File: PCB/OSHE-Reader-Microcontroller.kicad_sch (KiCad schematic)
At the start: 3 parts

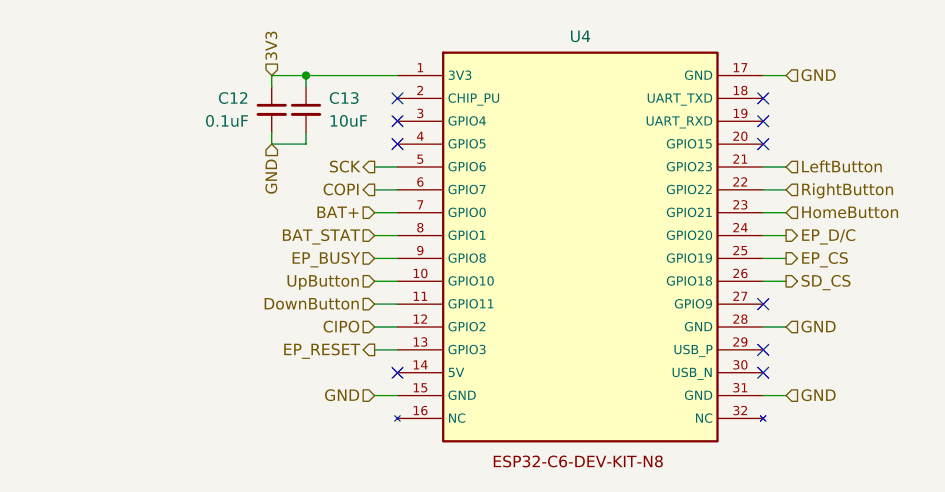
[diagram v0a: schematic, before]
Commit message: fixed battery voltage input to mcu being over 3.3V, minor changes to layout of sd card schematic
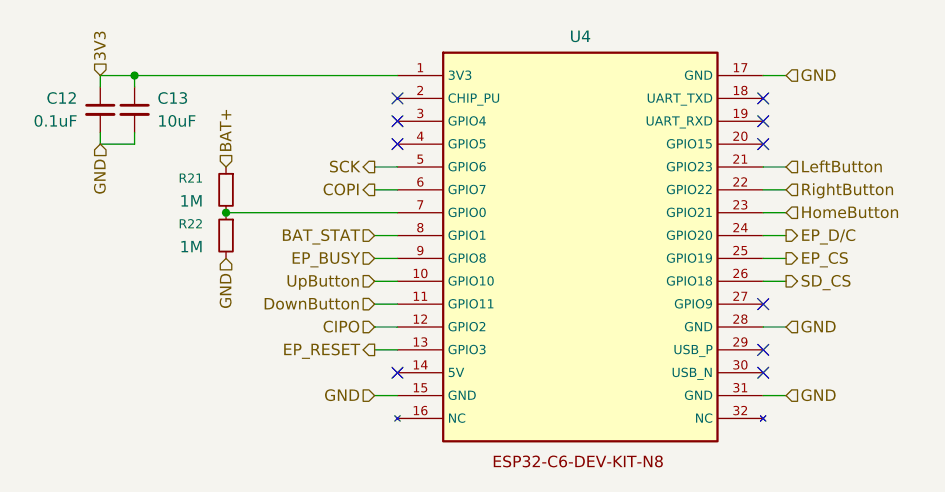
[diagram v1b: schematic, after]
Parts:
- added R21, R22: 1M, symbol Device:R_Small
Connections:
- net BAT+: now also R21.1; no longer U4.7 (GPIO0)
- net GND: now also R22.2
- new net: R21.2, R22.1, U4.7 (GPIO0)
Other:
- moved on the sheet: C12, C13
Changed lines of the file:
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@@
 	(paper "A4")
 	(junction
-		(at 53.34 49.53)
+		(at 34.29 49.53)
 		(diameter 0)
 		(color 0 0 0 0)
 	)
+	(junction
+		(at 44.45 64.77)
+		(diameter 0)
+		(color 0 0 0 0)
+	)
 	(no_connect
 		(at 63.5 54.61)
@@
 	(wire
 		(pts
-			(xy 49.53 49.53) (xy 53.34 49.53)
+			(xy 30.48 49.53) (xy 34.29 49.53)
 		)
 		(stroke
@@
 	(wire
 		(pts
-			(xy 53.34 50.8) (xy 53.34 49.53)
-		)
-		(stroke
-			(width 0)
-			(type default)
-		)
-	)
-	(wire
-		(pts
-			(xy 49.53 57.15) (xy 53.34 57.15)
+			(xy 34.29 50.8) (xy 34.29 49.53)
+		)
+		(stroke
+			(width 0)
+			(type default)
+		)
+	)
+	(wire
+		(pts
+			(xy 30.48 57.15) (xy 34.29 57.15)
 		)
 		(stroke
@@
 	(wire
 		(pts
+			(xy 44.45 64.77) (xy 63.5 64.77)
+		)
+		(stroke
+			(width 0)
+			(type default)
+		)
+	)
+	(wire
+		(pts
 			(xy 60.96 72.39) (xy 63.5 72.39)
 		)
@@
 	(wire
 		(pts
-			(xy 60.96 64.77) (xy 63.5 64.77)
-		)
-		(stroke
-			(width 0)
-			(type default)
-		)
-	)
-	(wire
-		(pts
 			(xy 60.96 62.23) (xy 63.5 62.23)
 		)
@@
 	(wire
 		(pts
-			(xy 49.53 57.15) (xy 49.53 55.88)
+			(xy 30.48 57.15) (xy 30.48 55.88)
 		)
 		(stroke
@@
 	(wire
 		(pts
-			(xy 49.53 50.8) (xy 49.53 49.53)
+			(xy 30.48 50.8) (xy 30.48 49.53)
 		)
 		(stroke
@@
 	(wire
 		(pts
-			(xy 53.34 57.15) (xy 53.34 55.88)
+			(xy 34.29 57.15) (xy 34.29 55.88)
 		)
 		(stroke
@@
 	(wire
 		(pts
-			(xy 53.34 49.53) (xy 63.5 49.53)
+			(xy 34.29 49.53) (xy 63.5 49.53)
 		)
 		(stroke
@@
 	(hierarchical_label "GND"
 		(shape input)
-		(at 49.53 57.15 270)
+		(at 30.48 57.15 270)
 		(effects
 			(font
@@
 	(hierarchical_label "BAT+"
 		(shape input)
-		(at 60.96 64.77 180)
-		(effects
-			(font
-				(size 1.27 1.27)
-			)
-			(justify right)
+		(at 44.45 59.69 90)
+		(effects
+			(font
+				(size 1.27 1.27)
+			)
+			(justify left)
 		)
 	)
@@
 	(hierarchical_label "3V3"
 		(shape input)
-		(at 49.53 49.53 90)
+		(at 30.48 49.53 90)
 		(effects
 			(font
@@
 		(shape output)
 		(at 60.96 59.69 180)
+		(effects
+			(font
+				(size 1.27 1.27)
+			)
+			(justify right)
+		)
+	)
+	(hierarchical_label "GND"
+		(shape input)
+		(at 44.45 69.85 270)
 		(effects
 			(font
@@
 	(symbol
 		(lib_id "Device:C_Small")
-		(at 49.53 53.34 0)
+		(at 30.48 53.34 0)
 		(mirror y)
 		(unit 1)
@@
 		(dnp no)
 		(property "Reference" "C12"
-			(at 46.99 52.0762 0)
+			(at 27.94 52.0762 0)
 			(effects
 				(font
@@
 		)
 		(property "Value" "0.1uF"
-			(at 46.99 54.6162 0)
+			(at 27.94 54.6162 0)
 			(effects
 				(font
@@
 		)
 		(property "Footprint" ""
-			(at 49.53 53.34 0)
+			(at 30.48 53.34 0)
 			(effects
 				(font
@@
 		)
 		(property "Datasheet" "~"
-			(at 49.53 53.34 0)
+			(at 30.48 53.34 0)
 			(effects
 				(font
@@
 		)
 		(property "Description" "Unpolarized capacitor, small symbol"
-			(at 49.53 53.34 0)
+			(at 30.48 53.34 0)
 			(effects
 				(font
@@
 	)
 	(symbol
+		(lib_id "Device:R_Small")
+		(at 44.45 67.31 0)
+		(mirror y)
+		(unit 1)
+		(exclude_from_sim no)
+		(in_bom yes)
+		(on_board yes)
+		(dnp no)
+		(property "Reference" "R22"
+			(at 41.91 66.0399 0)
+			(effects
+				(font
+					(size 1.016 1.016)
+				)
+				(justify left)
+			)
+		)
+		(property "Value" "1M"
+			(at 41.91 68.5799 0)
+			(effects
+				(font
+					(size 1.27 1.27)
+				)
+				(justify left)
+			)
+		)
+		(property "Footprint" ""
+			(at 44.45 67.31 0)
+			(effects
+				(font
+					(size 1.27 1.27)
+				)
+				(hide yes)
+			)
+		)
+		(property "Datasheet" "~"
+			(at 44.45 67.31 0)
+			(effects
+				(font
+					(size 1.27 1.27)
+				)
+				(hide yes)
+			)
+		)
+		(property "Description" "Resistor, small symbol"
+			(at 44.45 67.31 0)
+			(effects
+				(font
+					(size 1.27 1.27)
+				)
+				(hide yes)
+			)
+		)
+		(pin "1"
+		)
+		(pin "2"
+		)
+		(instances
+			(project "OSHE-Reader-PCB"
+				(path "/3f072c92-e35a-4654-839b-728bd3dc3a46/03424bf7-051b-4358-a08a-8020da2e6def"
+					(reference "R22")
+					(unit 1)
+				)
+			)
+		)
+	)
+	(symbol
+		(lib_id "Device:R_Small")
+		(at 44.45 62.23 0)
+		(mirror y)
+		(unit 1)
+		(exclude_from_sim no)
+		(in_bom yes)
+		(on_board yes)
+		(dnp no)
+		(property "Reference" "R21"
+			(at 41.91 60.9599 0)
+			(effects
+				(font
+					(size 1.016 1.016)
+				)
+				(justify left)
+			)
+		)
+		(property "Value" "1M"
+			(at 41.91 63.4999 0)
+			(effects
+				(font
+					(size 1.27 1.27)
+				)
+				(justify left)
+			)
+		)
+		(property "Footprint" ""
+			(at 44.45 62.23 0)
+			(effects
+				(font
+					(size 1.27 1.27)
+				)
+				(hide yes)
+			)
+		)
+		(property "Datasheet" "~"
+			(at 44.45 62.23 0)
+			(effects
+				(font
+					(size 1.27 1.27)
+				)
+				(hide yes)
+			)
+		)
+		(property "Description" "Resistor, small symbol"
+			(at 44.45 62.23 0)
+			(effects
+				(font
+					(size 1.27 1.27)
+				)
+				(hide yes)
+			)
+		)
+		(pin "1"
+		)
+		(pin "2"
+		)
+		(instances
+			(project ""
+				(path "/3f072c92-e35a-4654-839b-728bd3dc3a46/03424bf7-051b-4358-a08a-8020da2e6def"
+					(reference "R21")
+					(unit 1)
+				)
+			)
+		)
+	)
+	(symbol
 		(lib_id "Device:C_Small")
-		(at 53.34 53.34 0)
+		(at 34.29 53.34 0)
 		(unit 1)
 		(exclude_from_sim no)
@@
 		(dnp no)
 		(property "Reference" "C13"
-			(at 55.88 52.0762 0)
+			(at 36.83 52.0762 0)
 			(effects
 				(font
@@
 		)
 		(property "Value" "10uF"
-			(at 55.88 54.6162 0)
+			(at 36.83 54.6162 0)
 			(effects
 				(font
@@
 		)
 		(property "Footprint" ""
-			(at 53.34 53.34 0)
+			(at 34.29 53.34 0)
 			(effects
 				(font
@@
 		)
 		(property "Datasheet" "~"
-			(at 53.34 53.34 0)
+			(at 34.29 53.34 0)
 			(effects
 				(font
@@
 		)
 		(property "Description" "Unpolarized capacitor, small symbol"
-			(at 53.34 53.34 0)
-			(effects
-				(font
+			(at 34.29 53.34 0)
+			(effects
+				(font

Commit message: Footprints added
All footprints added (problem with J1 for some reason) ((pads of the display driver))
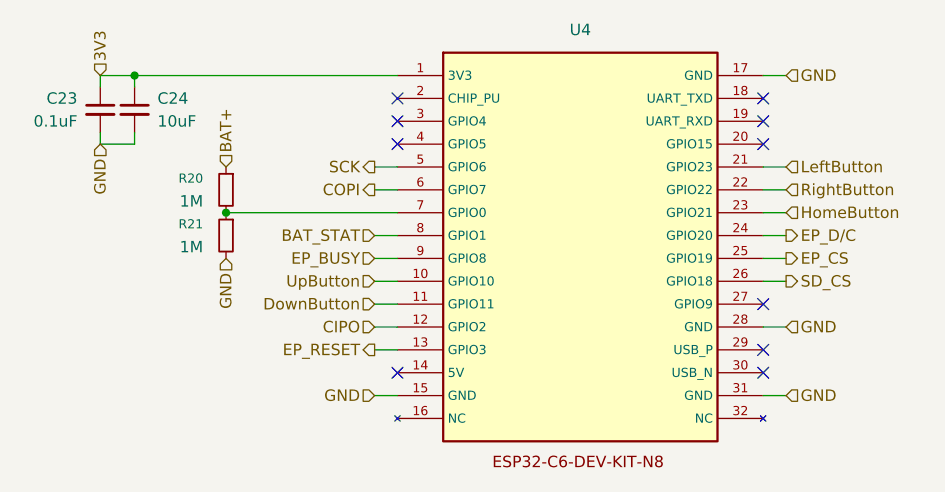
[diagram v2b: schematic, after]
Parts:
- C23: renamed from C12; footprint (none) -> Capacitor_SMD:C_1206_3216Metric
- C24: renamed from C13; footprint (none) -> Capacitor_SMD:C_1206_3216Metric
- R20: renamed from R21; footprint (none) -> Resistor_SMD:R_1206_3216Metric
- R21: renamed from R22; footprint (none) -> Resistor_SMD:R_1206_3216Metric
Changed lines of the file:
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@@
 		(fields_autoplaced yes)
 		(property "Reference" "U4"
-			(at 83.82 45.212 0)
+			(at 83.82 44.45 0)
 			(effects
 				(font
@@
 			(project ""
 				(path "/3f072c92-e35a-4654-839b-728bd3dc3a46/03424bf7-051b-4358-a08a-8020da2e6def"
+					(reference "U4")
+					(unit 1)
+				)
+			)
+			(project "OSHE-Reader-Microcontroller"
+				(path "/45bff31a-189b-4ed1-b273-a8e68dfd337a"
 					(reference "U4")
 					(unit 1)
@@
 		(on_board yes)
 		(dnp no)
-		(property "Reference" "C12"
+		(property "Reference" "C23"
 			(at 27.94 52.0762 0)
 			(effects
@@
 			)
 		)
-		(property "Footprint" ""
+		(property "Footprint" "Capacitor_SMD:C_1206_3216Metric"
 			(at 30.48 53.34 0)
 			(effects
@@
 				(path "/3f072c92-e35a-4654-839b-728bd3dc3a46/03424bf7-051b-4358-a08a-8020da2e6def"
 					(reference "C12")
+					(unit 1)
+				)
+			)
+			(project "OSHE-Reader-Microcontroller"
+				(path "/45bff31a-189b-4ed1-b273-a8e68dfd337a"
+					(reference "C23")
 					(unit 1)
 				)
@@
 		(on_board yes)
 		(dnp no)
-		(property "Reference" "R22"
+		(property "Reference" "R21"
 			(at 41.91 66.0399 0)
 			(effects
@@
 			)
 		)
-		(property "Footprint" ""
+		(property "Footprint" "Resistor_SMD:R_1206_3216Metric"
 			(at 44.45 67.31 0)
 			(effects
@@
 				(path "/3f072c92-e35a-4654-839b-728bd3dc3a46/03424bf7-051b-4358-a08a-8020da2e6def"
 					(reference "R22")
+					(unit 1)
+				)
+			)
+			(project "OSHE-Reader-Microcontroller"
+				(path "/45bff31a-189b-4ed1-b273-a8e68dfd337a"
+					(reference "R21")
 					(unit 1)
 				)
@@
 		(on_board yes)
 		(dnp no)
-		(property "Reference" "R21"
+		(property "Reference" "R20"
 			(at 41.91 60.9599 0)
 			(effects
@@
 			)
 		)
-		(property "Footprint" ""
+		(property "Footprint" "Resistor_SMD:R_1206_3216Metric"
 			(at 44.45 62.23 0)
 			(effects
@@
 				(path "/3f072c92-e35a-4654-839b-728bd3dc3a46/03424bf7-051b-4358-a08a-8020da2e6def"
 					(reference "R21")
+					(unit 1)
+				)
+			)
+			(project "OSHE-Reader-Microcontroller"
+				(path "/45bff31a-189b-4ed1-b273-a8e68dfd337a"
+					(reference "R20")
 					(unit 1)
 				)
@@
 		(on_board yes)
 		(dnp no)
-		(property "Reference" "C13"
+		(property "Reference" "C24"
 			(at 36.83 52.0762 0)
 			(effects
@@
 			)
 		)
-		(property "Footprint" ""
+		(property "Footprint" "Capacitor_SMD:C_1206_3216Metric"
 			(at 34.29 53.34 0)
 			(effects
@@
 				)
 			)
-		)
-	)
+			(project "OSHE-Reader-Microcontroller"
+				(path "/45bff31a-189b-4ed1-b273-a8e68dfd337a"
+					(reference "C24")
+					(unit 1)
+				)
+			)
+		)
+	)
+	(sheet_instances
+		(path "/"
+			(page "1")
+		)
+	)
+	(embedded_fonts no)
 )
